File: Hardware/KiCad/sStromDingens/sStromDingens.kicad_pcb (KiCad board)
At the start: 2 copper layers, 16 x 44.2 mm, 27 parts, among them J1 LiPo+ (2S-3S), J2 LED, J3 LiPo- (2S-3S), J7 RC, U1 AL8862SP-13, U2 CH32V003J4M6, U3 AMS1117-3.3

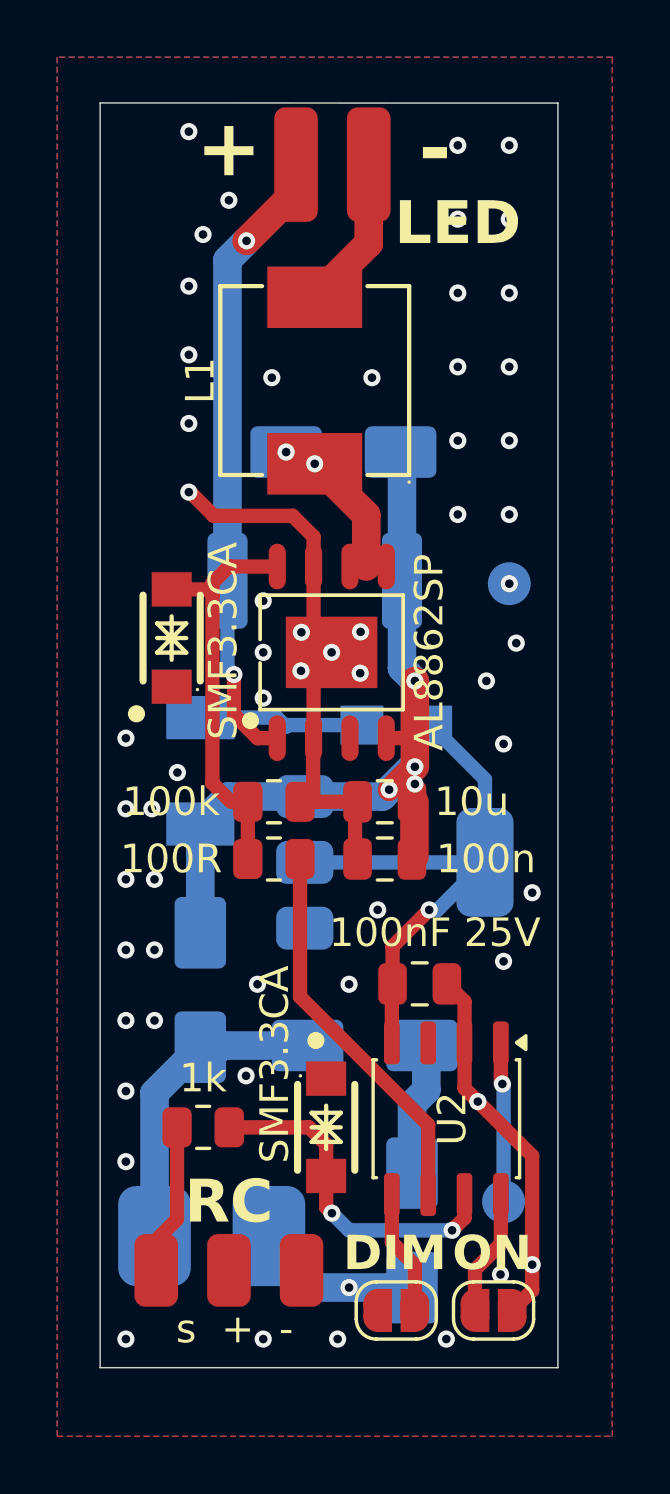
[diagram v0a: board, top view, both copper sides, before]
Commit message: Hardware v2.0: Add TVS protection, move Failsafe to Pin 1
- Add SMF3.3CA TVS diodes for input protection (LiPo)
- Add SMAJ26CA TVS diode for LED output protection
- Remove SMAJ15A overvoltage protection
- Move Failsafe jumper from Pin 8 (PD4) to Pin 1 (PD6)
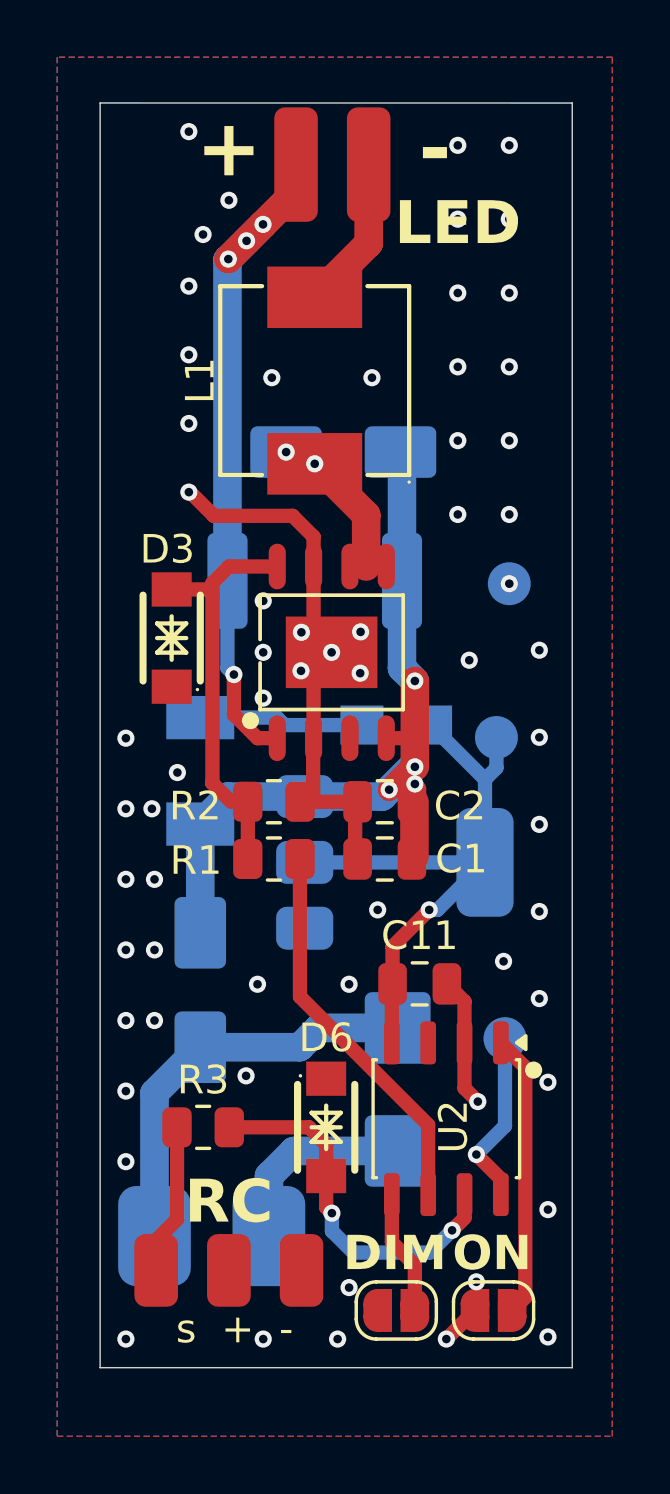
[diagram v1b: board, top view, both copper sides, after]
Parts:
- removed D4, D5: SMAJ15A, Diode_SMD:D_SMA
- added D8: SMAJ26CA, Diode_SMD:D_SMB, B.Cu at (119.9, 95.3)
- added TP3: 3V3, TestPoint:TestPoint_Pad_D1.5mm, B.Cu at (123.3, 83.0)
- J1: value LiPo+ (2S-3S) -> LiPo+ (2S-6S)
- J3: value LiPo- (2S-3S) -> LiPo- (2S-6S)
- moved TP1 5.70 mm to (123.7, 93.5)
- turned JP2 to 0 degrees
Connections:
- U2 pad 1: /SWIO -> Net-(JP2-B)
- U2 pad 8: Net-(JP2-B) -> /SWIO
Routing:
- net Net-(JP2-B): track 4.42 -> 9.90 mm
- net GND: track 43.5 -> 38.1 mm, vias 59 -> 63
- net Net-(D4-A1): track 4.07 -> 0.00 mm
- net Net-(D7-A): track 10.7 -> 14.3 mm
- net /SET: track 22.2 -> 23.9 mm, vias 2 -> 4
- net 3,3V: track 19.7 -> 21.3 mm
- net /RC_Signal: track 12.0 -> 13.0 mm
- net /SWIO: track 5.59 -> 6.22 mm
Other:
- board size 16 x 44.2 mm -> 16.5 x 44.2 mm
- board text added: "2S-6S"
- board text added: "V0giK 03/2026"
- board text added: "sStromDingens 2.0"
- board text removed: "2S/3S"
- board text removed: "AL8862SP"
- board text removed: "V0giK 02/2026"
- board text removed: "sStromDingens 1.0"

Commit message: Docs/Hardware: LiPo-Spec von 6S auf 4S korrigiert (AMS1117 max. 15V)
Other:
- board text added: "2S-4S"
- board text removed: "2S-6S"
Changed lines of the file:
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@@
 		)
 	)
-	(gr_text "2S-6S"
+	(gr_text "2S-4S"
 		(at 113.6 97.15 0)
 		(layer "B.SilkS" knockout)

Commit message: Fix: Verbleibende 6S/26V-Referenzen auf 4S/16.8V korrigiert
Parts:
- J1: value LiPo+ (2S-6S) -> LiPo+ (2S-4S)
- J3: value LiPo- (2S-6S) -> LiPo- (2S-4S)
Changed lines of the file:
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@@
 		(sheetname "/")
 		(sheetfile "sStromDingens.kicad_sch")
-		(attr through_hole)
+		(attr through_hole exclude_from_bom)
 		(pad "1" smd roundrect
 			(at 0 0 90)
@@
 		(sheetname "/")
 		(sheetfile "sStromDingens.kicad_sch")
-		(attr through_hole)
+		(attr through_hole exclude_from_bom)
 		(pad "1" smd roundrect
 			(at 0 0 90)
@@
 			)
 		)
-		(property "Value" "LiPo+ (2S-6S)"
+		(property "Value" "LiPo+ (2S-4S)"
 			(at 0.1 1.77 90)
 			(layer "B.Fab")
@@
 			)
 		)
-		(property "Value" "LiPo- (2S-6S)"
+		(property "Value" "LiPo- (2S-4S)"
 			(at 0.1 1.77 90)
 			(layer "B.Fab")
